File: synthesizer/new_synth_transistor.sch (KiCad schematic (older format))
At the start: 28 parts, among them J1 Conn_ARM_JTAG_SWD_10, Q1 2N3904, Q2 2N3904, Q3 2N3904, Q4 2N3904, U1 7402, U3 LM324, U4 STM32F072RBTx

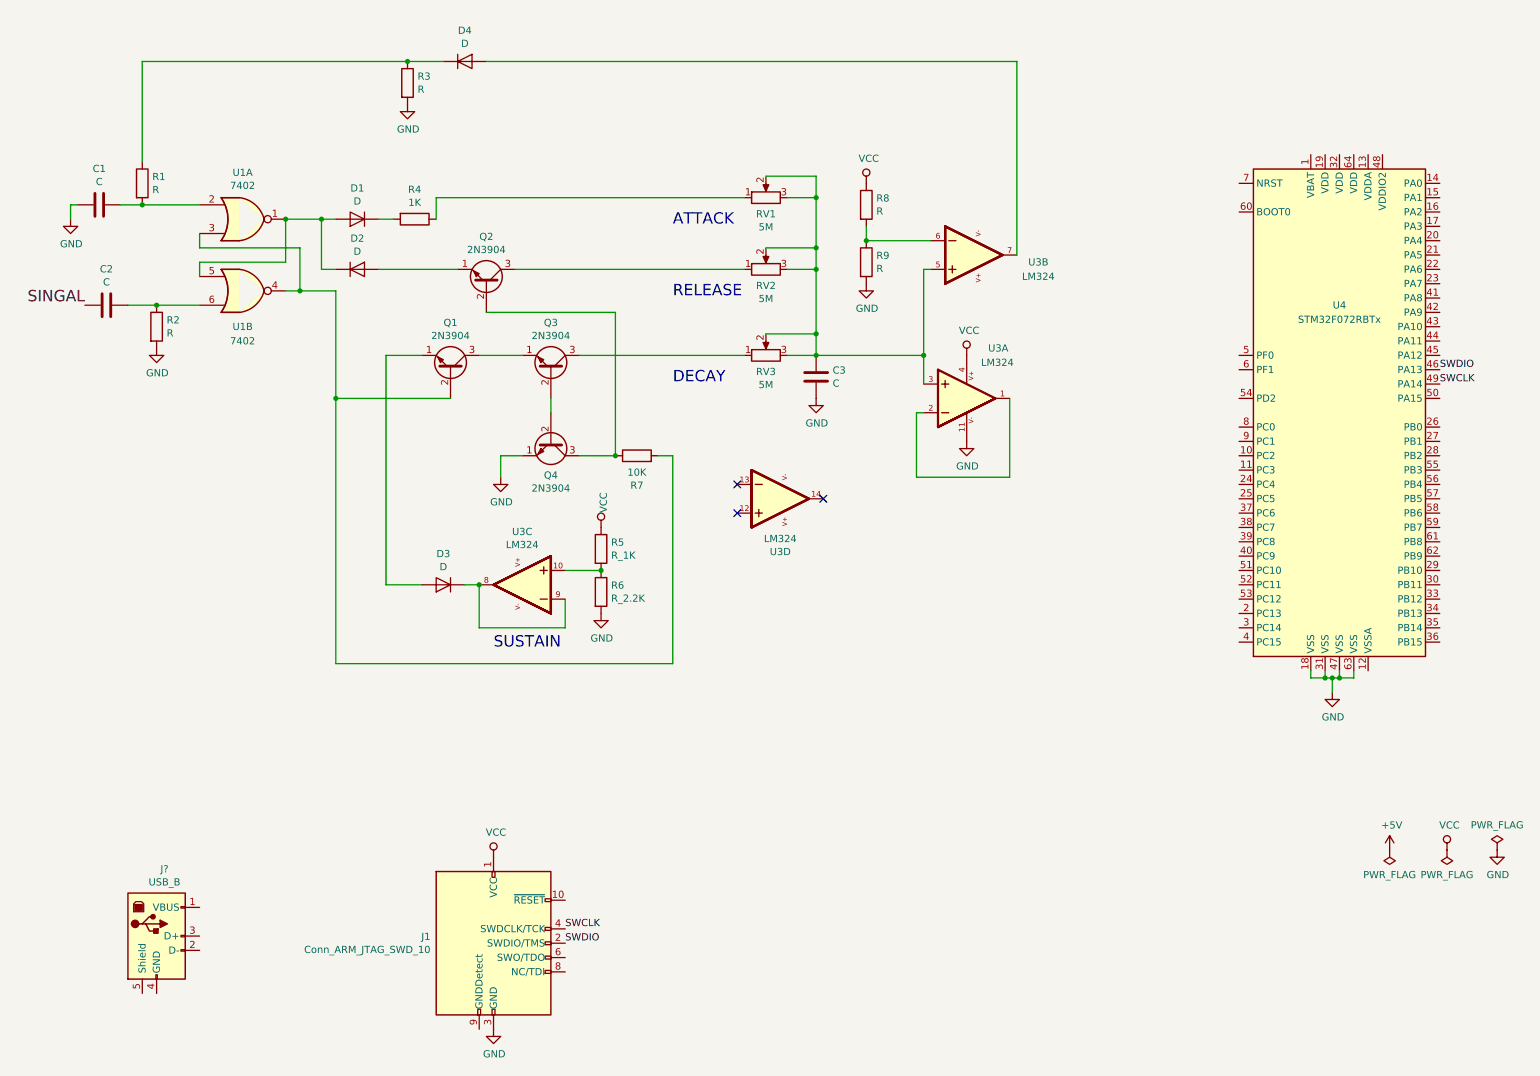
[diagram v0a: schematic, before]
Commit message: Update STM32 Chip
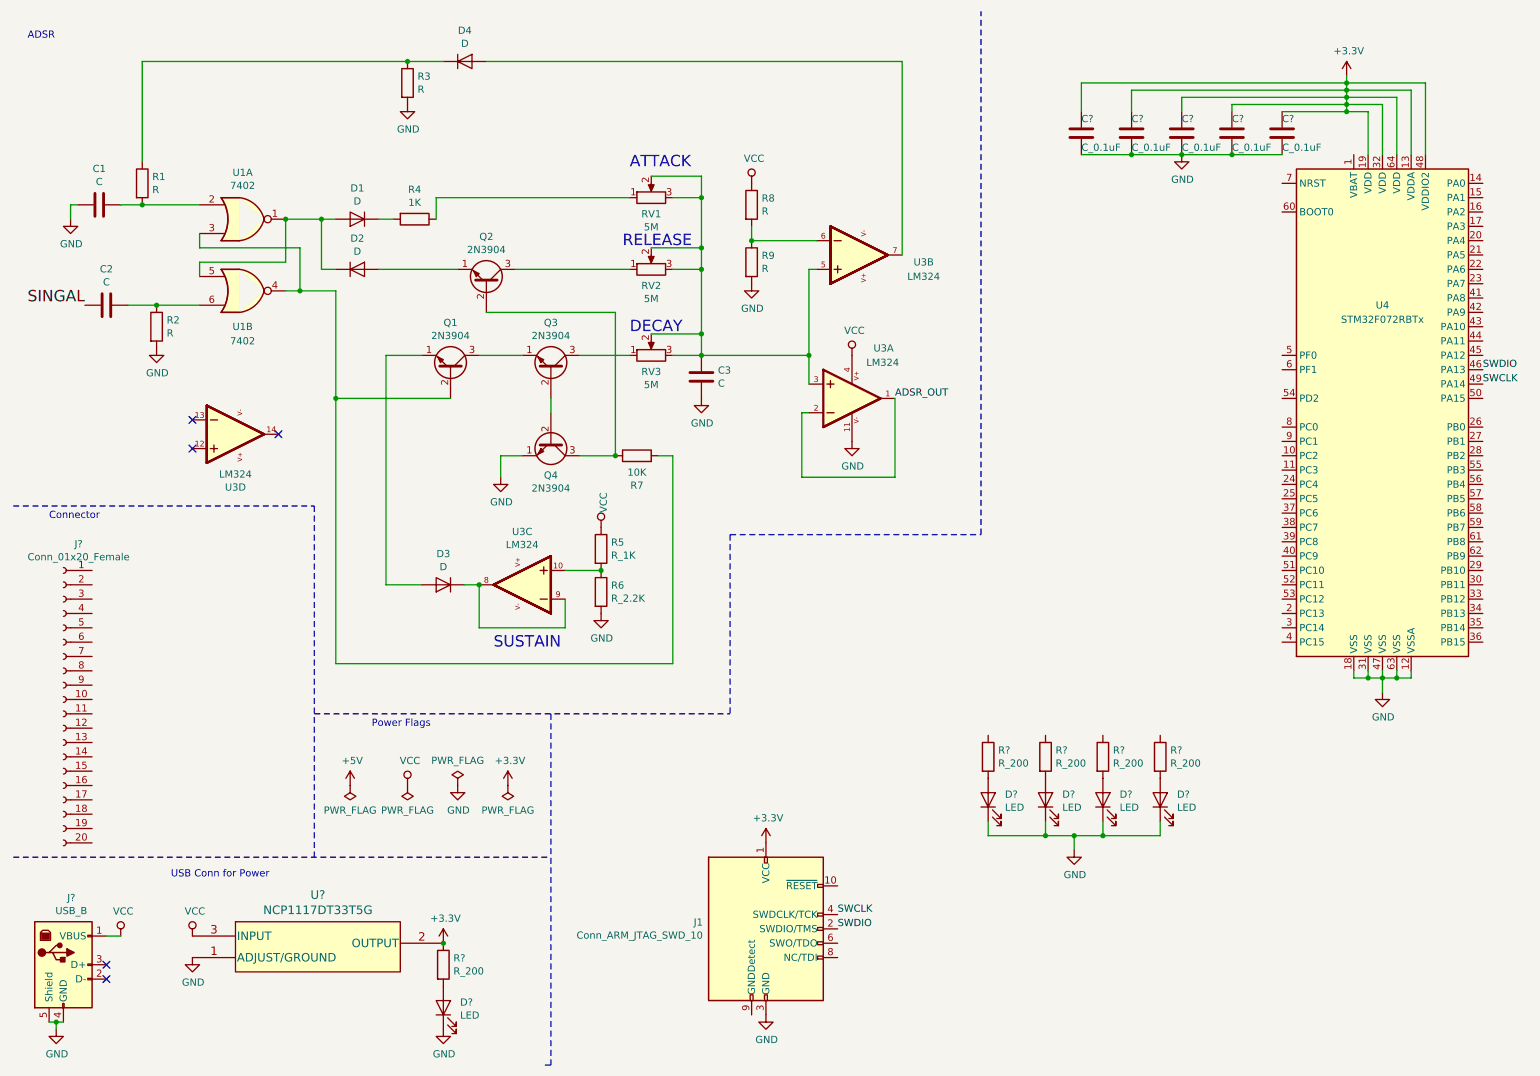
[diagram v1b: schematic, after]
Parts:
- added C? (x5): C_0.1uF, symbol Device:C
- added D? (x5): LED, symbol Device:LED
- added J?: Conn_01x20_Female, symbol Connector:Conn_01x20_Female
- added R? (x5): R_200, symbol Device:R
- added U?: NCP1117DT33T5G, NCP1117:NCP1117DT33T5G, symbol NCP1117DT33T5G:NCP1117DT33T5G
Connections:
- net GND: now also J?.4 (GND), J?.5 (Shield), U4.12 (VSSA), C?.2, C?.2, C?.2, C?.2, C?.2, D?.1 (K), D?.1 (K), D?.1 (K), D?.1 (K), D?.1 (K), U?.1 (ADJUST/GROUND)
- net VCC: now also J?.1 (VBUS), U?.3 (INPUT); no longer J1.1 (VCC)
- net +3V3: now reaches U4.13 (VDDA)
- net +3V3: now also J1.1 (VCC), U4.19 (VDD), U4.32 (VDD), U4.48 (VDDIO2), U4.64 (VDD), C?.1, C?.1, C?.1, C?.1, C?.1, R?.1, U?.2 (OUTPUT)
- net ADSR_OUT: now reaches U3.1 (OUTPUT1), U3.2 (INVERTING_INPUT1)
- new net: D?.2 (A), R?.2 (x5)
- no-connect marks 3 -> 5
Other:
- note added: "ADSR\n"
- note added: "Connector\n"
- note added: "Power Flags\n"
- note added: "USB Conn for Power\n"
- moved on the sheet: C3, J1, J?, R8, R9, RV1, RV2, RV3, U3A, U3B, U3D, U4

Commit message: Final Schematic
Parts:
- removed Q1, Q2, Q3, Q4: 2N3904, Package_TO_SOT_THT:TO-92_Inline, symbol Transistor_BJT:2N3904
- removed R8, R9: R, symbol Device:R
- removed RV1, RV2, RV3: 5M, symbol Device:R_POT
- added Q? (x4): MMBT3904, Package_TO_SOT_SMD:SOT-23, symbol Transistor_BJT:MMBT3904
- added R? (x3): R_200, symbol Device:R
- added R? (x3): R, symbol Device:R
- C1, C2: value C -> C_1nF
- C3: value C -> C_2.2uF
- R1, R2: value R -> R_1M
- R3: value R -> R_499K
- R4: value 1K -> R_1K
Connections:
- net GND: now also R1.1, Q?.2 (E); no longer C1.2
- net VCC: now also U3.6 (INVERTING_INPUT2)
- net at R7.2, U1.3, U1.4: now also R?.2
- net at D4.1 (K), R3.1: now also C1.2; no longer R1.1
- net at R4.1: now also R?.2
- net at C3.1, U3.3 (NON-INVERTING_INPUT1), U3.5 (NON-INVERTING_INPUT2): now also R?.1, R?.1, R?.1
- net at D3.2 (A): now also Q?.2 (E)
- net at D2.2 (A): now also Q?.2 (E)
- net at R7.1: now also Q?.3 (C), R?.1
- net SINGAL renamed SIGNAL
- net SIGNAL: now also R?.2
- new net: Q?.1 (B), R?.2
- new net: Q?.1 (B), Q?.1 (B), R?.1
- new net: Q?.1 (B), R?.1
- new net: Q?.3 (C), R?.2 (x2)
- new net: Q?.2 (E), Q?.3 (C)
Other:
- moved on the sheet: C1, R1, U3D
